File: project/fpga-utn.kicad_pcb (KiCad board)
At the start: 2 copper layers, 129 parts, among them P1 Conector SMD 2x10, P2 Conector SMD 2x10, P3 Conector SMD 2x10, P4 Conector SMD 2x10, U1 LD1117S33TR_SOT223, U2 LD1117S12TR_SOT223, U3 USBLC6-2SC6, U4 FT2232HL, U5 M93C66, U6 ICE40HX4K-TQ144, U7 W25X40CLSN, Y1 ECS-3225MV-120-CN-TR, Y2 ECS-3225MVQ-1000-CN-TR

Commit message: Agregados footprints de todos los componentes
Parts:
- added D10: LED Red, 150141RS73100(LED):LEDM3528X210N, F.Cu at (58.2, 100.8)
- added D11: LED Red, 150141RS73100(LED):LEDM3528X210N, F.Cu at (58.2, 104.8)
- added D12: LED Red, 150141RS73100(LED):LEDM3528X210N, F.Cu at (58.2, 108.8)
- added D2: LED Green, 150141RS73100(LED):LEDM3528X210N, F.Cu at (66.0, 80.8)
- added D4: LED Red, 150141RS73100(LED):LEDM3528X210N, F.Cu at (66.0, 86.8)
- added D5: LED Green, 150141RS73100(LED):LEDM3528X210N, F.Cu at (58.2, 80.8)
- added D6: LED Green, 150141RS73100(LED):LEDM3528X210N, F.Cu at (58.2, 84.8)
- added D7: LED Green, 150141RS73100(LED):LEDM3528X210N, F.Cu at (58.2, 88.8)
- added D8: LED Green, 150141RS73100(LED):LEDM3528X210N, F.Cu at (58.2, 92.8)
- added D9: LED Red, 150141RS73100(LED):LEDM3528X210N, F.Cu at (58.2, 96.8)
- added J1: USB_C_Receptacle_USB2.0_16P, GSB1C41110SSHR:GSB1C41110SSHR, F.Cu at (140.2, 97.7)
- added SW1: SW_Push, TS04_66_75_BK_100_SMT:SW_TS04-66-75-BK-100-SMT, F.Cu at (198.5, 58.8)
- added SW2: SW_Push, TS04_66_75_BK_100_SMT:SW_TS04-66-75-BK-100-SMT, F.Cu at (198.5, 66.4)
- added SW3: SW_Push, TS04_66_75_BK_100_SMT:SW_TS04-66-75-BK-100-SMT, F.Cu at (198.5, 73.9)
- added SW4: SW_Push, TS04_66_75_BK_100_SMT:SW_TS04-66-75-BK-100-SMT, F.Cu at (198.5, 81.5)
- added SW5: SW_Push, TS04_66_75_BK_100_SMT:SW_TS04-66-75-BK-100-SMT, F.Cu at (198.5, 89.0)
- added SW6: SW_Push, TS04_66_75_BK_100_SMT:SW_TS04-66-75-BK-100-SMT, F.Cu at (198.5, 96.6)
- added SW7: SW_Push, TS04_66_75_BK_100_SMT:SW_TS04-66-75-BK-100-SMT, F.Cu at (198.5, 104.1)
- added SW8: SW_Push, TS04_66_75_BK_100_SMT:SW_TS04-66-75-BK-100-SMT, F.Cu at (198.5, 111.7)
- D3: footprint Diode_SMD:D_1206_3216Metric -> Diode_SMD:D_1206_3216Metric_Pad1.42x1.75mm_HandSolder
- FB1, FB2, FB3, FB4, FB5: footprint Diode_SMD:D_1206_3216Metric -> Inductor_SMD:L_1206_3216Metric_Pad1.42x1.75mm_HandSolder
- moved D3 109.2 mm to (209.9, 56.8)
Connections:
- TP6 pad 1: Net-(U4-OSCI) -> /Perifericos/12MHz_CLK
- U4 pad 2: Net-(U4-OSCI) -> /Perifericos/12MHz_CLK
- U6 pad 52: unconnected-(U6C-IOB_82_GBIN4-Pad52) -> /Perifericos/12MHz_CLK
- Y1 pad 3: Net-(U4-OSCI) -> /Perifericos/12MHz_CLK

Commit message: PCB etapa de potencia y comunicacion lista
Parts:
- removed the TP1 at (84.3, 92.6)
- removed the TP2 at (84.3, 97.2)
- removed the TP3 at (84.3, 101.7)
- removed TP4: TP4_GND, TestPoint:TestPoint_Pad_D2.5mm
- moved D12 187.2 mm to (236.5, 51.5), turned to 90 degrees
- moved D11 182.2 mm to (232.5, 51.5), turned to 90 degrees
- moved D10 177.3 mm to (228.5, 51.5), turned to 90 degrees
- moved D9 172.3 mm to (224.5, 51.5), turned to 90 degrees
- moved D8 167.4 mm to (220.5, 51.5), turned to 90 degrees
- moved D7 162.6 mm to (216.5, 51.5), turned to 90 degrees
- moved D6 158.3 mm to (212.9, 51.5), turned to 90 degrees
- moved D5 153.5 mm to (208.9, 51.5), turned to 90 degrees
- moved U6 117.4 mm to (201.8, 90.2), turned to 180 degrees
- moved C12 111.3 mm to (210.2, 64.0), turned to -90 degrees
- moved D2 106.6 mm to (168.6, 51.5), turned to 90 degrees
- moved U4 102.7 mm to (199.0, 60.8)
- moved C15 102.7 mm to (207.2, 59.0), turned to 90 degrees
- moved R8 100.6 mm to (196.2, 51.5), turned to -90 degrees
- moved R7 100.3 mm to (198.8, 51.5), turned to -90 degrees
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- renumbered TP6 to TP1, TP5 to TP2, TP7 to TP3
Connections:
- U6 pad 110: /Perifericos/LED1 -> unconnected-(U6A-IOT_168-Pad110)
- U6 pad 112: /Perifericos/LED2 -> unconnected-(U6A-IOT_169-Pad112)
- U6 pad 113: /Perifericos/LED3 -> unconnected-(U6A-IOT_170-Pad113)
- U6 pad 114: /Perifericos/LED4 -> unconnected-(U6A-IOT_171-Pad114)
- U6 pad 115: /Perifericos/LED5 -> unconnected-(U6A-IOT_172-Pad115)
- U6 pad 116: /Perifericos/LED6 -> unconnected-(U6A-IOT_173-Pad116)
- U6 pad 117: /Perifericos/LED7 -> unconnected-(U6A-IOT_174-Pad117)
- U6 pad 118: /Perifericos/LED8 -> unconnected-(U6A-IOT_177-Pad118)
- U6 pad 37: unconnected-(U6C-IOB_56-Pad37) -> /Perifericos/LED1
- U6 pad 38: unconnected-(U6C-IOB_57-Pad38) -> /Perifericos/LED2
- U6 pad 39: unconnected-(U6C-IOB_61-Pad39) -> /Perifericos/LED3
- U6 pad 41: unconnected-(U6C-IOB_63-Pad41) -> /Perifericos/LED4
- U6 pad 42: unconnected-(U6C-IOB_64-Pad42) -> /Perifericos/LED5
- U6 pad 43: unconnected-(U6C-IOB_71-Pad43) -> /Perifericos/LED6
- U6 pad 44: unconnected-(U6C-IOB_72-Pad44) -> /Perifericos/LED7
- U6 pad 45: unconnected-(U6C-IOB_73-Pad45) -> /Perifericos/LED8
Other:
- board outline added: 100 x 75 mm

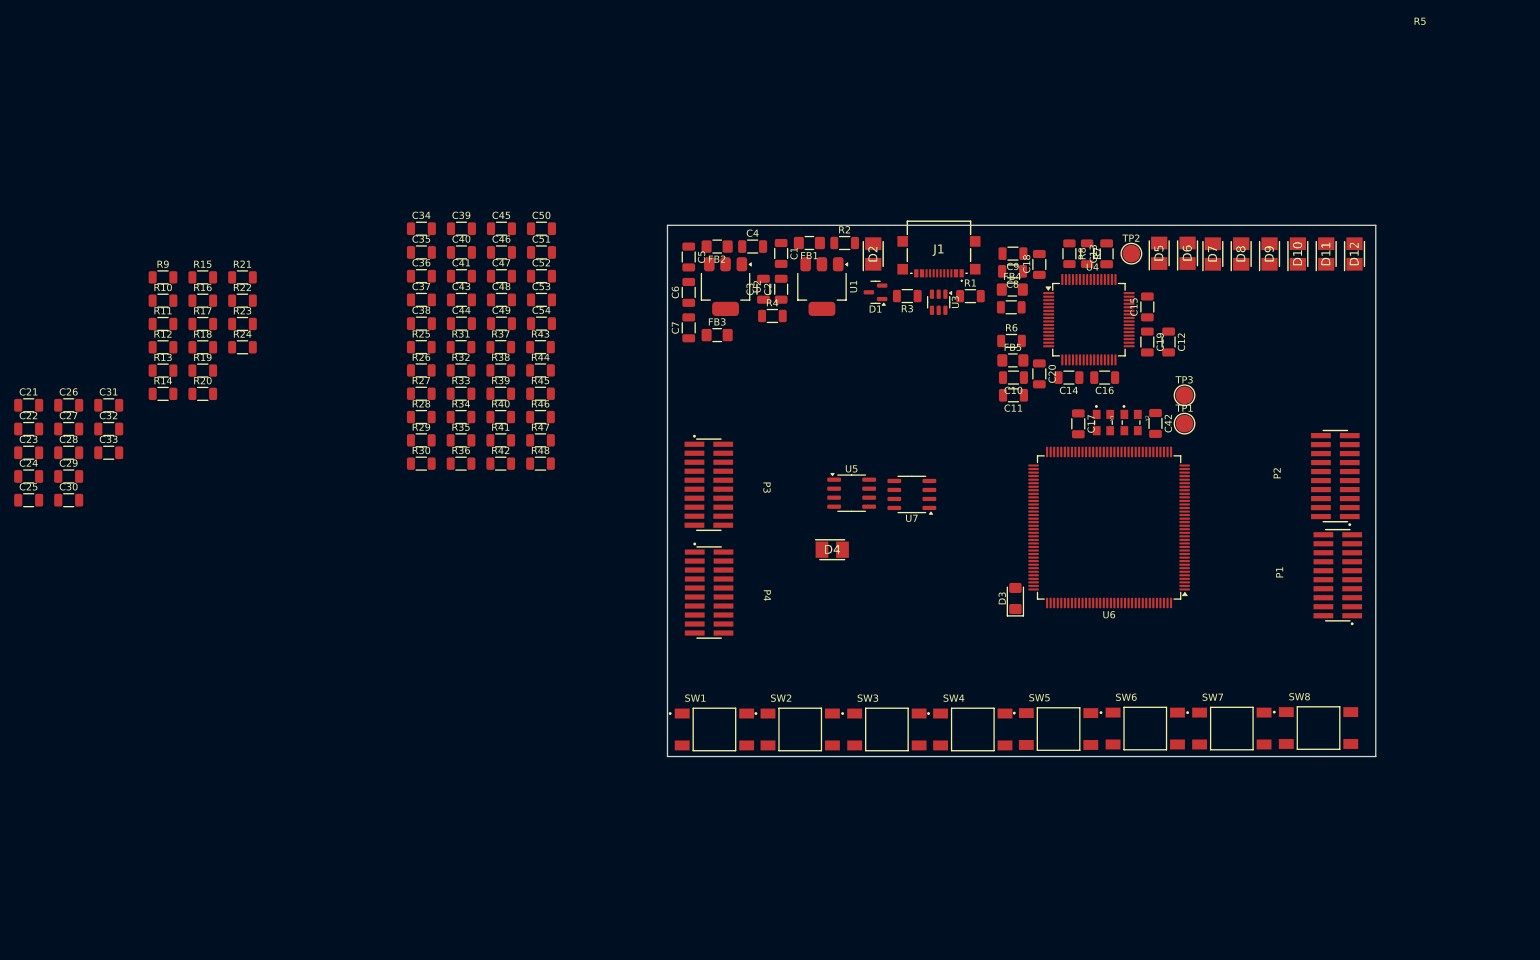
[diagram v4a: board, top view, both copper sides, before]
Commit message: Componentes colocados, version 1
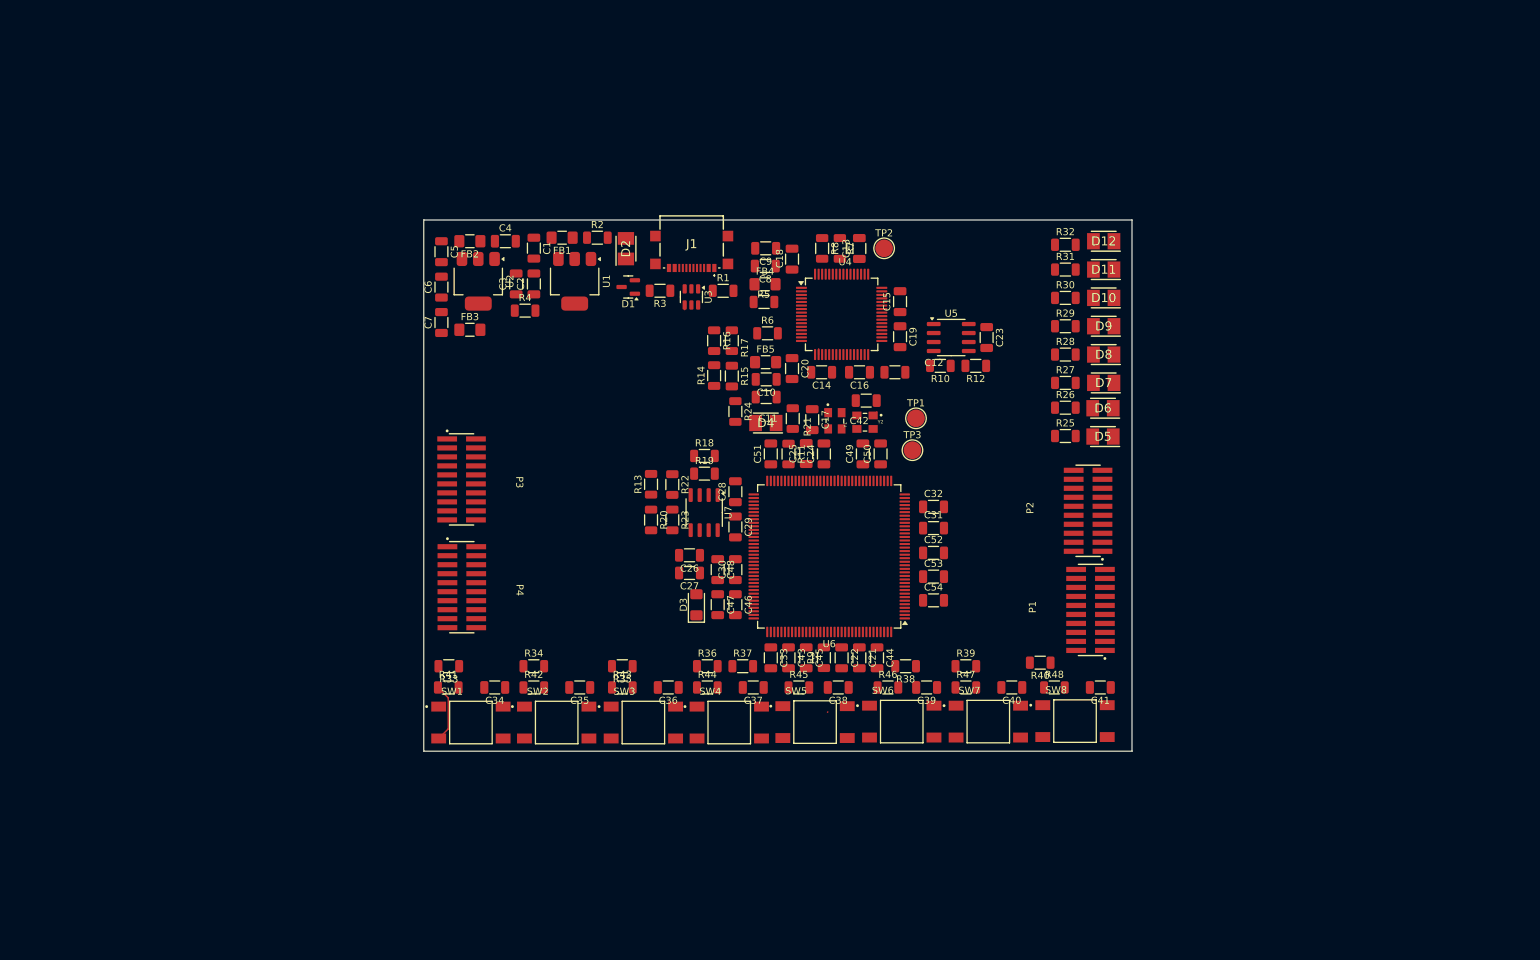
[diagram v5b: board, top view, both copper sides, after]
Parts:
- moved C23 136.2 mm to (184.6, 63.3), turned to -90 degrees
- moved C21 122.6 mm to (166.6, 108.6), turned to -90 degrees
- moved C22 119.2 mm to (164.1, 108.6), turned to -90 degrees
- moved C31 117.7 mm to (177.1, 90.2)
- moved C32 117.0 mm to (177.1, 87.2)
- moved R12 114.8 mm to (183.0, 67.3), turned to 180 degrees
- moved C24 112.3 mm to (161.6, 79.8), turned to 90 degrees
- moved R10 110.1 mm to (178.0, 67.3), turned to 180 degrees
- moved C25 110.0 mm to (159.1, 79.7), turned to 90 degrees
- moved R9 107.7 mm to (161.6, 108.5), turned to 90 degrees
- moved C41 107.3 mm to (200.6, 112.8), turned to 180 degrees
- moved C40 99.0 mm to (188.1, 112.8), turned to 180 degrees
- moved C33 97.9 mm to (154.1, 108.6), turned to -90 degrees
- moved C30 94.6 mm to (149.1, 96.1), turned to 90 degrees
- moved C29 94.4 mm to (149.1, 90.1), turned to -90 degrees
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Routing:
- net Net-(R33-Pad2): track 0.00 -> 8.36 mm
- net +3V3: track 0.00 -> 1.40 mm
- net /Memorias y PLL/Flash_DO: track 0.00 -> 0.81 mm
- net /Perifericos/12MHz_CLK: track 0.00 -> 0.77 mm
- net /Power Supply/D+: track 0.00 -> 0.66 mm
- net GND: track 0.00 -> 0.51 mm
- net Net-(R37-Pad2): track 0.00 -> 0.50 mm

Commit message: Version 1 pcb, sin finalizar
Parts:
- removed C10, C13, C14, C15, C16, C18, C19, C20, C23, C8: 100n, Capacitor_SMD:C_1206_3216Metric
- removed C11, C9: 4u7, Capacitor_SMD:C_1206_3216Metric
- removed C12: 3u3, Capacitor_SMD:C_1206_3216Metric
- removed C26: 10n, Capacitor_SMD:C_1206_3216Metric
- removed C27: 1u, Capacitor_SMD:C_1206_3216Metric
- removed FB4, FB5: FerriteBead_Small, Inductor_SMD:L_1206_3216Metric_Pad1.42x1.75mm_HandSolder
- removed R10: 2k2, Resistor_SMD:R_1206_3216Metric
- removed R12, R13, R19, R20, R7, R8: 10k, Resistor_SMD:R_1206_3216Metric
- removed R14, R22, R23: 220, Resistor_SMD:R_1206_3216Metric
- removed R15, R16, R17, R18: R, Resistor_SMD:R_1206_3216Metric
- removed R5: 12k, Resistor_SMD:R_1206_3216Metric
- removed R6: 1k, Resistor_SMD:R_1206_3216Metric
- removed TP1: 12MHZ, TestPoint:TestPoint_Pad_D2.5mm
- removed TP2: TP_PWR_EN, TestPoint:TestPoint_Pad_D2.5mm
- removed TP3: 100MHZ, TestPoint:TestPoint_Pad_D2.5mm
- removed U7: W25X40CLSN, Package_SO:SOIC-8_3.9x4.9mm_P1.27mm
- P1, P2, P3, P4: footprint FRT-FPGA:Header 2x10 SMD -> Connector_PinSocket_2.54mm:PinSocket_2x10_P2.54mm_Vertical
- moved P3 122.5 mm to (219.5, 139.7), turned to 180 degrees
- moved P4 109.7 mm to (219.5, 113.0), turned to 180 degrees
- moved P2 71.5 mm to (133.3, 116.8), turned to 0 degrees
- moved U4 66.8 mm to (196.5, 118.5)
- moved P1 66.6 mm to (133.3, 90.2), turned to 0 degrees
- moved C1 60.7 mm to (173.0, 81.5), turned to 90 degrees
- moved C42 59.0 mm to (155.5, 130.1), turned to 0 degrees
- moved FB1 56.1 mm to (170.5, 81.5), turned to 90 degrees
- moved R24 56.0 mm to (176.5, 122.6), turned to 180 degrees
- moved R21 55.6 mm to (177.5, 126.5), turned to 90 degrees
- moved D4 55.4 mm to (174.5, 126.6), turned to 90 degrees
- moved C2 53.9 mm to (168.0, 81.5), turned to -90 degrees
- moved C3 53.9 mm to (165.5, 81.5), turned to -90 degrees
- moved Y2 53.1 mm to (155.5, 127.0), turned to 0 degrees
- moved C5 52.8 mm to (151.5, 80.5), turned to 0 degrees
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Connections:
- U6 pad 1: Net-(U6D-IOL_2A) -> Net-(P1-IO1)
- U6 pad 10: Net-(U6D-IOL_5B) -> Net-(P1-IO8)
- U6 pad 101: Net-(U6B-IOR_160) -> Net-(P4-IO9)
- U6 pad 102: Net-(U6B-IOR_161) -> Net-(P4-IO10)
- U6 pad 104: Net-(U6B-IOR_164) -> Net-(P4-IO11)
- U6 pad 105: Net-(U6B-IOR_165) -> Net-(P4-IO12)
- U6 pad 106: Net-(U6B-IOR_166) -> Net-(P4-IO13)
- U6 pad 107: Net-(U6B-IOR_167) -> Net-(P4-IO14)
- U6 pad 11: Net-(U6D-IOL_8A) -> Net-(P1-IO9)
- U6 pad 110: unconnected-(U6A-IOT_168-Pad110) -> /Perifericos/LED1
- U6 pad 112: unconnected-(U6A-IOT_169-Pad112) -> /Perifericos/LED2
- U6 pad 113: unconnected-(U6A-IOT_170-Pad113) -> /Perifericos/LED3
- U6 pad 114: unconnected-(U6A-IOT_171-Pad114) -> /Perifericos/LED4
- U6 pad 115: unconnected-(U6A-IOT_172-Pad115) -> /Perifericos/LED5
- U6 pad 116: unconnected-(U6A-IOT_173-Pad116) -> /Perifericos/LED6
- U6 pad 117: unconnected-(U6A-IOT_174-Pad117) -> /Perifericos/LED7
- U6 pad 118: unconnected-(U6A-IOT_177-Pad118) -> /Perifericos/LED8
- U6 pad 12: Net-(U6D-IOL_8B) -> Net-(P1-IO10)
- U6 pad 129: unconnected-(U6A-IOT_198_GBIN0-Pad129) -> /Perifericos/12MHz_CLK
- U6 pad 136: /Perifericos/BOT8 -> unconnected-(U6A-IOT_214-Pad136)
- U6 pad 137: /Perifericos/BOT7 -> unconnected-(U6A-IOT_215-Pad137)
- U6 pad 138: /Perifericos/BOT6 -> unconnected-(U6A-IOT_216-Pad138)
- U6 pad 139: /Perifericos/BOT5 -> unconnected-(U6A-IOT_217-Pad139)
- U6 pad 141: /Perifericos/BOT4 -> unconnected-(U6A-IOT_219-Pad141)
- U6 pad 142: /Perifericos/BOT3 -> unconnected-(U6A-IOT_220-Pad142)
- U6 pad 143: /Perifericos/BOT2 -> unconnected-(U6A-IOT_221-Pad143)
- U6 pad 144: /Perifericos/BOT1 -> unconnected-(U6A-IOT_222-Pad144)
- U6 pad 15: Net-(U6D-IOL_10A) -> Net-(P1-IO11)
- U6 pad 16: Net-(U6D-IOL_10B) -> Net-(P1-IO12)
- U6 pad 17: Net-(U6D-IOL_12A) -> Net-(P1-IO13)
- U6 pad 18: Net-(U6D-IOL_12B) -> Net-(P1-IO14)
- U6 pad 19: Net-(U6D-IOL_13A) -> Net-(P2-IO1)
- U6 pad 2: Net-(U6D-IOL_2B) -> Net-(P1-IO2)
- U6 pad 20: Net-(U6D-IOL_13B_GBIN7) -> Net-(P2-IO2)
- U6 pad 21: Net-(U6D-IOL_14A_GBIN6) -> Net-(P2-IO3)
- U6 pad 22: Net-(U6D-IOL_14B) -> Net-(P2-IO4)
- U6 pad 23: Net-(U6D-IOL_17A) -> Net-(P2-IO5)
- U6 pad 24: Net-(U6D-IOL_17B) -> Net-(P2-IO6)
- U6 pad 25: Net-(U6D-IOL_18A) -> Net-(P2-IO7)
- U6 pad 26: Net-(U6D-IOL_18B) -> Net-(P2-IO8)
- U6 pad 28: Net-(U6D-IOL_23A) -> Net-(P2-IO9)
- U6 pad 29: Net-(U6D-IOL_23B) -> Net-(P2-IO10)
- U6 pad 3: Net-(U6D-IOL_3A) -> Net-(P1-IO3)
- U6 pad 31: Net-(U6D-IOL_24A) -> Net-(P2-IO11)
- U6 pad 32: Net-(U6D-IOL_24B) -> Net-(P2-IO12)
- U6 pad 33: Net-(U6D-IOL_25A) -> Net-(P2-IO13)
- U6 pad 34: Net-(U6D-IOL_25B) -> Net-(P2-IO14)
- U6 pad 37: /Perifericos/LED1 -> /Perifericos/BOT1
- U6 pad 38: /Perifericos/LED2 -> /Perifericos/BOT2
- U6 pad 39: /Perifericos/LED3 -> /Perifericos/BOT3
- U6 pad 4: Net-(U6D-IOL_3B) -> Net-(P1-IO4)
- U6 pad 41: /Perifericos/LED4 -> /Perifericos/BOT4
- U6 pad 42: /Perifericos/LED5 -> /Perifericos/BOT5
- U6 pad 43: /Perifericos/LED6 -> /Perifericos/BOT6
- U6 pad 44: /Perifericos/LED7 -> /Perifericos/BOT7
- U6 pad 45: /Perifericos/LED8 -> /Perifericos/BOT8
- U6 pad 52: /Perifericos/12MHz_CLK -> unconnected-(U6C-IOB_82_GBIN4-Pad52)
- U6 pad 7: Net-(U6D-IOL_4A) -> Net-(P1-IO5)
- U6 pad 73: Net-(U6B-IOR_109) -> Net-(P3-IO1)
- U6 pad 74: Net-(U6B-IOR_110) -> Net-(P3-IO2)
- U6 pad 75: Net-(U6B-IOR_111) -> Net-(P3-IO3)
- U6 pad 76: Net-(U6B-IOR_112) -> Net-(P3-IO4)
- U6 pad 78: Net-(U6B-IOR_114) -> Net-(P3-IO5)
- U6 pad 79: Net-(U6B-IOR_115) -> Net-(P3-IO6)
- U6 pad 8: Net-(U6D-IOL_4B) -> Net-(P1-IO6)
- U6 pad 80: Net-(U6B-IOR_116) -> Net-(P3-IO7)
- U6 pad 81: Net-(U6B-IOR_117) -> Net-(P3-IO8)
- U6 pad 82: Net-(U6B-IOR_118) -> Net-(P3-IO9)
- U6 pad 83: Net-(U6B-IOR_119) -> Net-(P3-IO10)
- U6 pad 84: Net-(U6B-IOR_120) -> Net-(P3-IO11)
- U6 pad 85: Net-(U6B-IOR_128) -> Net-(P3-IO12)
- U6 pad 87: Net-(U6B-IOR_136) -> Net-(P3-IO13)
- U6 pad 88: Net-(U6B-IOR_137) -> Net-(P3-IO14)
- U6 pad 9: Net-(U6D-IOL_5A) -> Net-(P1-IO7)
- U6 pad 91: Net-(U6B-IOR_139) -> Net-(P4-IO1)
- U6 pad 93: Net-(U6B-IOR_140_GBIN3) -> Net-(P4-IO2)
- U6 pad 94: Net-(U6B-IOR_141_GBIN2) -> Net-(P4-IO3)
- U6 pad 95: Net-(U6B-IOR_144) -> Net-(P4-IO4)
- U6 pad 96: Net-(U6B-IOR_146) -> Net-(P4-IO5)
- U6 pad 97: Net-(U6B-IOR_147) -> Net-(P4-IO6)
- U6 pad 98: Net-(U6B-IOR_148) -> Net-(P4-IO7)
- U6 pad 99: Net-(U6B-IOR_152) -> Net-(P4-IO8)
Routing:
- net GND: track 0.51 -> 351.6 mm, vias 0 -> 8
- net +3V3: track 1.40 -> 344.0 mm
- net +5V: track 0.00 -> 275.3 mm, vias 0 -> 1
- net /Perifericos/BOT6: track 0.00 -> 79.1 mm, vias 0 -> 2
- net /Perifericos/BOT8: track 0.00 -> 75.3 mm, vias 0 -> 2
- net Net-(P3-IO6): track 0.00 -> 72.8 mm, vias 0 -> 1
- net Net-(P3-IO5): track 0.00 -> 72.0 mm, vias 0 -> 1
- net Net-(P4-IO2): track 0.00 -> 69.1 mm, vias 0 -> 1
- net Net-(P3-IO8): track 0.00 -> 68.2 mm, vias 0 -> 1
- net /Perifericos/BOT7: track 0.00 -> 67.9 mm, vias 0 -> 2
- net Net-(P3-IO7): track 0.00 -> 67.5 mm, vias 0 -> 1
- net Net-(P4-IO12): track 0.00 -> 66.0 mm, vias 0 -> 1
- net Net-(P4-IO4): track 0.00 -> 65.9 mm, vias 0 -> 1
- net Net-(P4-IO11): track 0.00 -> 64.6 mm, vias 0 -> 1
- net Net-(P4-IO3): track 0.00 -> 64.6 mm, vias 0 -> 1
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
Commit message: Ruteo critico finalizado
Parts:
- added C10: 100n, Capacitor_SMD:C_1206_3216Metric, F.Cu at (186.3, 125.3)
- added C11: 4u7, Capacitor_SMD:C_1206_3216Metric, F.Cu at (185.3, 127.9)
- added C12: 3u3, Capacitor_SMD:C_1206_3216Metric, F.Cu at (204.9, 118.5)
- added C13: 100n, Capacitor_SMD:C_1206_3216Metric, F.Cu at (193.3, 133.3)
- added C14: 100n, Capacitor_SMD:C_1206_3216Metric, F.Cu at (198.1, 133.5)
- added C15: 100n, Capacitor_SMD:C_1206_3216Metric, F.Cu at (205.7, 122.3)
- added C16: 100n, Capacitor_SMD:C_1206_3216Metric, F.Cu at (199.9, 115.8)
- added C18: 100n, Capacitor_SMD:C_1206_3216Metric, F.Cu at (186.3, 130.3)
- added C19: 100n, Capacitor_SMD:C_1206_3216Metric, F.Cu at (205.5, 126.2)
- added C20: 100n, Capacitor_SMD:C_1206_3216Metric, F.Cu at (195.1, 115.8)
- added C23: 100n, Capacitor_SMD:C_1206_3216Metric, F.Cu at (193.4, 97.9)
- added C26: 10n, Capacitor_SMD:C_1206_3216Metric, F.Cu at (198.6, 98.2)
- added C27: 1u, Capacitor_SMD:C_1206_3216Metric, F.Cu at (198.6, 100.7)
- added C8: 100n, Capacitor_SMD:C_1206_3216Metric, F.Cu at (186.1, 121.8)
- added C9: 4u7, Capacitor_SMD:C_1206_3216Metric, F.Cu at (186.1, 119.3)
- added FB4: FerriteBead_Small, Inductor_SMD:L_1206_3216Metric_Pad1.42x1.75mm_HandSolder, F.Cu at (186.1, 116.7)
- added FB5: FerriteBead_Small, Inductor_SMD:L_1206_3216Metric_Pad1.42x1.75mm_HandSolder, F.Cu at (186.0, 132.6)
- added R10: 2k2, Resistor_SMD:R_1206_3216Metric, F.Cu at (193.2, 112.1)
- added R12: 10k, Resistor_SMD:R_1206_3216Metric, F.Cu at (193.2, 109.3)
- added R13: 10k, Resistor_SMD:R_1206_3216Metric, F.Cu at (204.0, 90.0)
- added R14: 220, Resistor_SMD:R_1206_3216Metric, F.Cu at (180.0, 131.2)
- added R15: R, Resistor_SMD:R_1206_3216Metric, F.Cu at (203.8, 93.0)
- added R16: R, Resistor_SMD:R_1206_3216Metric, F.Cu at (190.1, 94.5)
- added R17: R, Resistor_SMD:R_1206_3216Metric, F.Cu at (203.6, 95.9)
- added R18: R, Resistor_SMD:R_1206_3216Metric, F.Cu at (189.7, 91.4)
- added R19: 10k, Resistor_SMD:R_1206_3216Metric, F.Cu at (194.0, 89.4)
- added R20: 10k, Resistor_SMD:R_1206_3216Metric, F.Cu at (207.4, 95.1)
- added R22: 220, Resistor_SMD:R_1206_3216Metric, F.Cu at (207.5, 89.7)
- added R23: 220, Resistor_SMD:R_1206_3216Metric, F.Cu at (209.9, 89.7)
- added R5: 12k, Resistor_SMD:R_1206_3216Metric, F.Cu at (190.1, 115.8)
- added R6: 1k, Resistor_SMD:R_1206_3216Metric, F.Cu at (189.7, 131.8)
- added R7: 10k, Resistor_SMD:R_1206_3216Metric, F.Cu at (186.4, 103.4)
- added R8: 10k, Resistor_SMD:R_1206_3216Metric, F.Cu at (189.5, 99.7)
- added TP2: TP_PWR_EN, TestPoint:TestPoint_Pad_D2.5mm, F.Cu at (208.9, 115.4)
- added U7: W25X40CLSN, Package_SO:SOIC-8_3.9x4.9mm_P1.27mm, F.Cu at (196.4, 93.9)
- moved C45 7.26 mm to (167.0, 90.8)
- moved U4 5.68 mm to (195.5, 124.1)
- moved U5 3.50 mm to (193.5, 105.3)
- moved D10 0.78 mm to (200.5, 77.2)
- moved D11 0.78 mm to (196.5, 77.2)
- moved D12 0.78 mm to (192.5, 77.2)
- moved D5 0.78 mm to (220.5, 77.2)
- moved D6 0.78 mm to (216.5, 77.2)
- moved D7 0.78 mm to (212.5, 77.2)
- moved D8 0.78 mm to (208.5, 77.2)
- moved D9 0.78 mm to (204.5, 77.2)
- moved R25 0.78 mm to (220.5, 82.7)
- moved R26 0.78 mm to (216.5, 82.7)
- moved R27 0.78 mm to (212.5, 82.7)
- moved R28 0.78 mm to (208.5, 82.7)
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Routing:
- net +3V3: track 344.0 -> 669.5 mm, vias 0 -> 11
- net +1V2: track 36.0 -> 161.4 mm, vias 0 -> 9
- net Net-(U6E-IOB_105_SDO): track 1.26 -> 89.8 mm, vias 1 -> 6
- net /Memorias y PLL/Flash_DO: track 0.00 -> 84.1 mm, vias 0 -> 2
- net /Memorias y PLL/Flash_CS: track 0.00 -> 82.6 mm, vias 0 -> 2
- net Net-(U6E-IOB_107_SCK): track 1.59 -> 84.0 mm, vias 1 -> 8
- net /Perifericos/VUART_DSR: track 1.26 -> 72.8 mm, vias 1 -> 2
- net /Perifericos/VUART_DCD: track 1.59 -> 71.7 mm, vias 1 -> 2
- net /Perifericos/VUART_Tx: track 0.00 -> 68.6 mm, vias 0 -> 2
- net /Perifericos/VUART_CTS: track 1.26 -> 68.2 mm, vias 1 -> 2
- net /Perifericos/VUART_DTR: track 1.59 -> 68.1 mm, vias 1 -> 2
- net Net-(U6E-IOB_106_SDI): track 1.59 -> 68.1 mm, vias 1 -> 6
- net /Perifericos/VUART_Rx: track 0.00 -> 63.6 mm, vias 0 -> 4
- net /Perifericos/VUART_RTS: track 1.59 -> 62.2 mm, vias 1 -> 2
- net Net-(U6E-IOB_108_SS): track 1.26 -> 60.2 mm, vias 1 -> 6
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
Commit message: Ruteado completo en V1
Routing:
- net GND: track 351.3 -> 556.1 mm, vias 12 -> 57
- net Net-(U6E-~{CRESET}): track 17.9 -> 90.1 mm, vias 2 -> 5
- net +1V8: track 35.0 -> 51.9 mm, vias 0 -> 3
- net /Perifericos/VUART_Rx: track 63.6 -> 70.6 mm
- net /Perifericos/VUART_DTR: track 68.1 -> 70.8 mm
- net /Perifericos/VUART_DCD: track 71.7 -> 73.3 mm
- net /Perifericos/VUART_DSR: track 72.8 -> 74.3 mm
- net /Perifericos/VUART_Tx: track 68.6 -> 69.7 mm
- net +5V: track 275.3 -> 276.4 mm
- net /Perifericos/VUART_RTS: track 62.2 -> 62.9 mm
- net +3V3: track 669.5 -> 669.3 mm, vias 11 -> 10
- added copper zone on B.Cu, net GND
